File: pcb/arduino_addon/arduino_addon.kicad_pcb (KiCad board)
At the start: 2 copper layers, 100 x 53 mm, 25 parts, among them P1 AnalogIn, P10 CONN_01X06, P2 Power, P3 Digital1, P4 Digital2, P5 BNC, P6 BNC, P7 BNC, P8 BNC, P9 BNC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

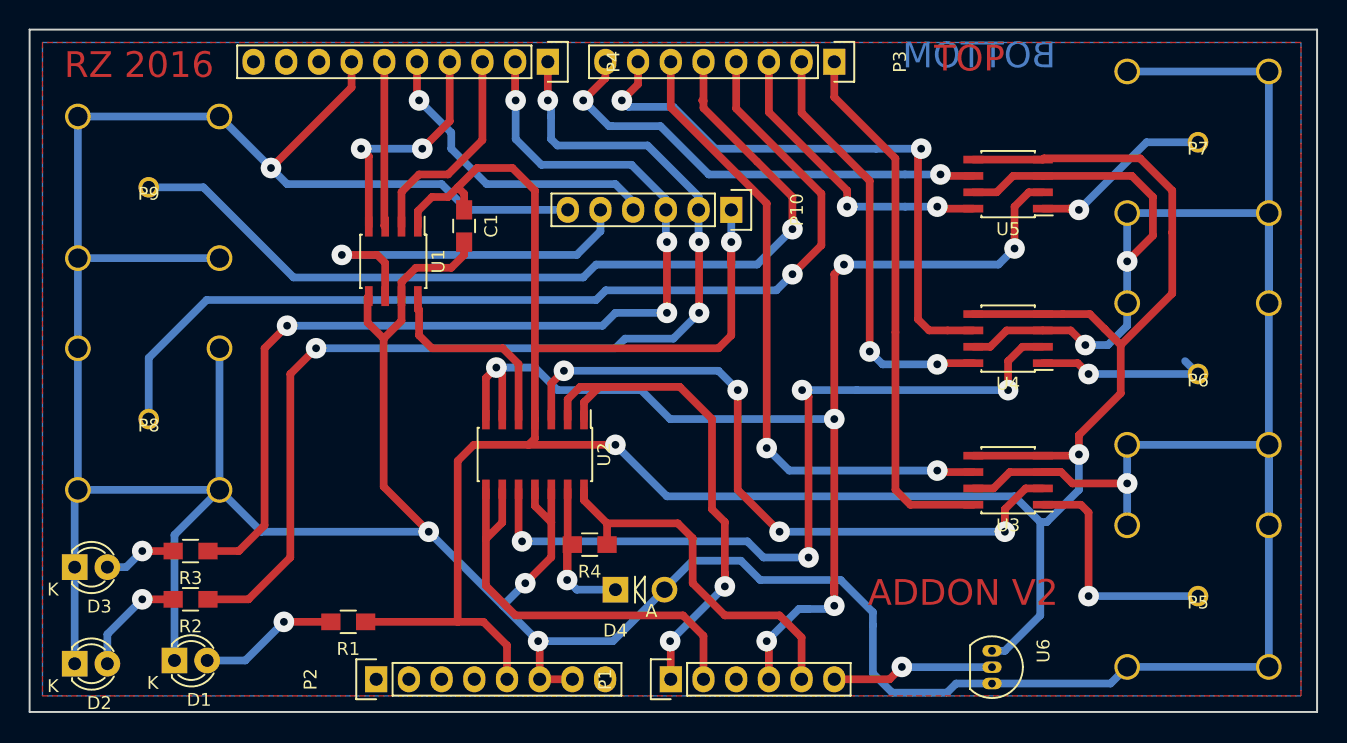
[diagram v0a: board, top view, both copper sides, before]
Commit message: footprint modifications, behav communication module initial version
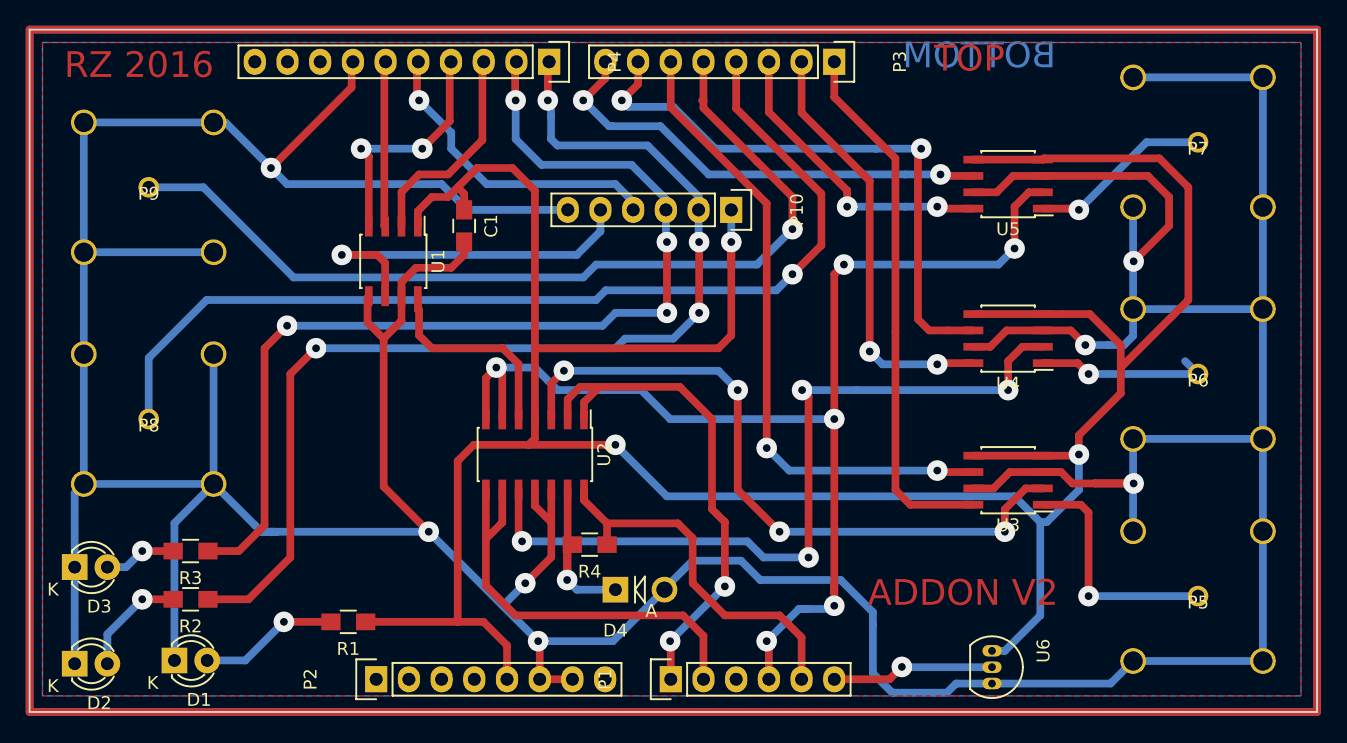
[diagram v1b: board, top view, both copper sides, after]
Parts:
- moved P4 0.10 mm to (140.3, 102.5)
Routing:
- net (no net): track 0.00 -> 612.0 mm
- net GND: track 446.5 -> 434.6 mm
- net +5V: track 216.0 -> 219.7 mm

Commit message: v2 pcb manufacturing files are generated
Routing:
- net /BNC1: track 13.8 -> 12.4 mm
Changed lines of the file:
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@@
     (thickness 1.6)
     (drawings 8)
-    (tracks 491)
+    (tracks 490)
     (zones 0)
     (modules 25)
@@
   (segment (start 100 153) (end 100 100) (width 0.6) (layer F.Cu) (net 0))
   (segment (start 200 153) (end 100 153) (width 0.6) (layer F.Cu) (net 0))
-  (segment (start 114.29 117.29) (end 104.21 117.29) (width 0.6) (layer B.Cu) (net 1) (status C00000))
-  (segment (start 114.29 135.29) (end 114.29 125.21) (width 0.6) (layer B.Cu) (net 1) (status C00000))
-  (segment (start 104.21 135.29) (end 104.21 107.21) (width 0.6) (layer B.Cu) (net 1) (status C00000))
-  (segment (start 104.21 107.21) (end 114.29 107.21) (width 0.6) (layer B.Cu) (net 1) (status C00000))
-  (segment (start 114.29 107.21) (end 114.33 107.25) (width 0.6) (layer B.Cu) (net 1) (status C00000))
-  (segment (start 114.33 107.25) (end 115.25 107.25) (width 0.6) (layer B.Cu) (net 1) (status C00000))
-  (segment (start 115.25 107.25) (end 118.75 110.75) (width 0.6) (layer B.Cu) (net 1) (status 400000))
-  (segment (start 103.5 149.25) (end 103.5 136) (width 0.6) (layer B.Cu) (net 1) (status 400000))
-  (segment (start 103.5 136) (end 104.21 135.29) (width 0.6) (layer B.Cu) (net 1) (status 800000))
-  (segment (start 111.25 149) (end 111.25 138.33) (width 0.6) (layer B.Cu) (net 1) (status 400000))
-  (segment (start 111.25 138.33) (end 114.29 135.29) (width 0.6) (layer B.Cu) (net 1) (status 800000))
-  (segment (start 114.29 135.29) (end 104.21 135.29) (width 0.6) (layer B.Cu) (net 1) (status C00000))
-  (segment (start 114.29 135.29) (end 117.5 138.5) (width 0.6) (layer B.Cu) (net 1) (status 400000))
+  (segment (start 114.29 117.29) (end 104.21 117.29) (width 0.6) (layer B.Cu) (net 1))
+  (segment (start 114.29 135.29) (end 114.29 125.21) (width 0.6) (layer B.Cu) (net 1))
+  (segment (start 104.21 135.29) (end 104.21 107.21) (width 0.6) (layer B.Cu) (net 1))
+  (segment (start 104.21 107.21) (end 114.29 107.21) (width 0.6) (layer B.Cu) (net 1))
+  (segment (start 114.29 107.21) (end 114.33 107.25) (width 0.6) (layer B.Cu) (net 1))
+  (segment (start 114.33 107.25) (end 115.25 107.25) (width 0.6) (layer B.Cu) (net 1))
+  (segment (start 115.25 107.25) (end 118.75 110.75) (width 0.6) (layer B.Cu) (net 1))
+  (segment (start 103.5 149.25) (end 103.5 136) (width 0.6) (layer B.Cu) (net 1))
+  (segment (start 103.5 136) (end 104.21 135.29) (width 0.6) (layer B.Cu) (net 1))
+  (segment (start 111.25 149) (end 111.25 138.33) (width 0.6) (layer B.Cu) (net 1))
+  (segment (start 111.25 138.33) (end 114.29 135.29) (width 0.6) (layer B.Cu) (net 1))
+  (segment (start 114.29 135.29) (end 104.21 135.29) (width 0.6) (layer B.Cu) (net 1))
+  (segment (start 114.29 135.29) (end 117.5 138.5) (width 0.6) (layer B.Cu) (net 1))
   (segment (start 117.5 138.5) (end 118 139) (width 0.6) (layer B.Cu) (net 1))
   (segment (start 118 139) (end 119 139) (width 0.6) (layer B.Cu) (net 1))
@@
   (segment (start 182 124.5) (end 183.75 124.5) (width 0.6) (layer B.Cu) (net 1))
   (segment (start 178.7 123.365) (end 180.865 123.365) (width 0.6) (layer F.Cu) (net 1))
-  (segment (start 185.71 123.79) (end 185.71 121.71) (width 0.6) (layer B.Cu) (net 1) (status 800000))
+  (segment (start 185.71 123.79) (end 185.71 121.71) (width 0.6) (layer B.Cu) (net 1))
   (segment (start 185 124.5) (end 185.71 123.79) (width 0.6) (layer B.Cu) (net 1))
   (segment (start 185.5 111.365) (end 186.865 111.365) (width 0.6) (layer F.Cu) (net 1))
@@
   (segment (start 185.71 118) (end 185.75 118) (width 0.6) (layer B.Cu) (net 1))
   (segment (start 185.75 118) (end 185.71 118) (width 0.6) (layer B.Cu) (net 1))
-  (segment (start 185.71 121.71) (end 195.79 121.71) (width 0.6) (layer B.Cu) (net 1) (status C00000))
-  (segment (start 185.71 113.79) (end 185.71 118) (width 0.6) (layer B.Cu) (net 1) (status 400000))
-  (segment (start 185.71 118) (end 185.71 121.71) (width 0.6) (layer B.Cu) (net 1) (status 800000))
+  (segment (start 185.71 121.71) (end 195.79 121.71) (width 0.6) (layer B.Cu) (net 1))
+  (segment (start 185.71 113.79) (end 185.71 118) (width 0.6) (layer B.Cu) (net 1))
+  (segment (start 185.71 118) (end 185.71 121.71) (width 0.6) (layer B.Cu) (net 1))
   (segment (start 182.75 135.25) (end 185.75 135.25) (width 0.6) (layer F.Cu) (net 1))
   (via (at 185.75 135.25) (size 1.6) (drill 0.6) (layers F.Cu B.Cu) (net 1))
@@
   (segment (start 182.25 126.75) (end 181.405 125.905) (width 0.6) (layer F.Cu) (net 8))
   (via (at 182.25 126.75) (size 1.6) (drill 0.6) (layers F.Cu B.Cu) (net 8))
-  (segment (start 190.75 126.75) (end 189.75 125.75) (width 0.6) (layer B.Cu) (net 8))
   (segment (start 186.75 108.75) (end 190.75 108.75) (width 0.6) (layer B.Cu) (net 9))
   (segment (start 181.5 114) (end 186.75 108.75) (width 0.6) (layer B.Cu) (net 9))
